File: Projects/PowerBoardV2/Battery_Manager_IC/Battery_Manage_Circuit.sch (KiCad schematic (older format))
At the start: 77 parts, among them J1 STATUS, J2 ROVER_PWR, Q1 FDG1024NZ, Q2 CSD17578Q5A, Q3 CSD17578Q5A, Q4 BSS138, SW1 SW_PUSH, U1 S-8244, U2 ATmega16HVB

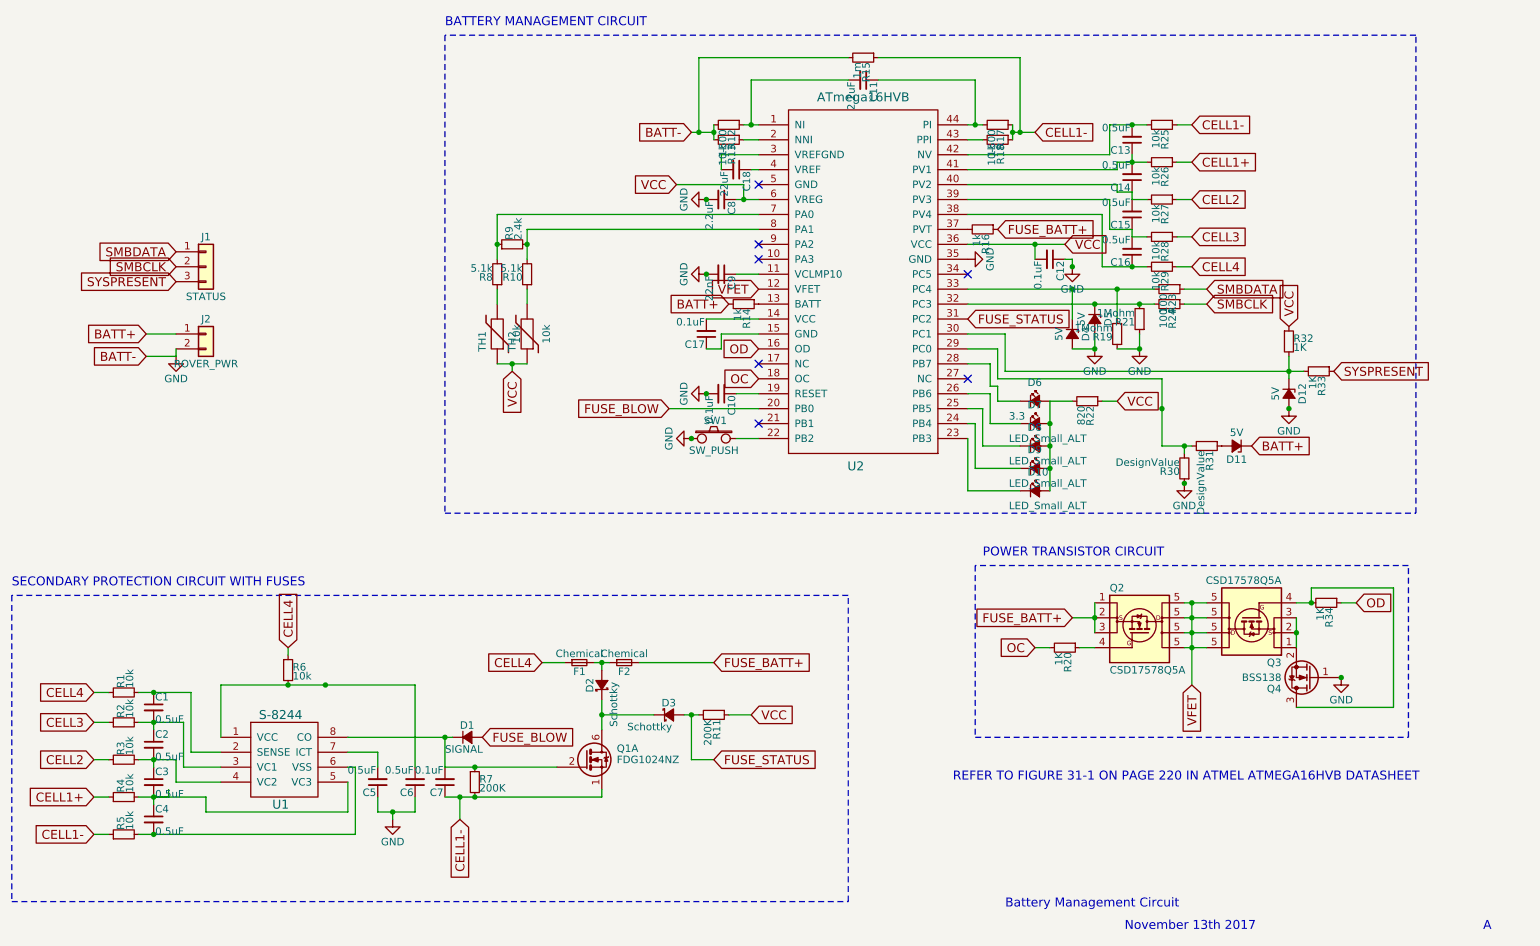
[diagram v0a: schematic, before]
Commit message: New Datasheets
Added new datasheets to the folder
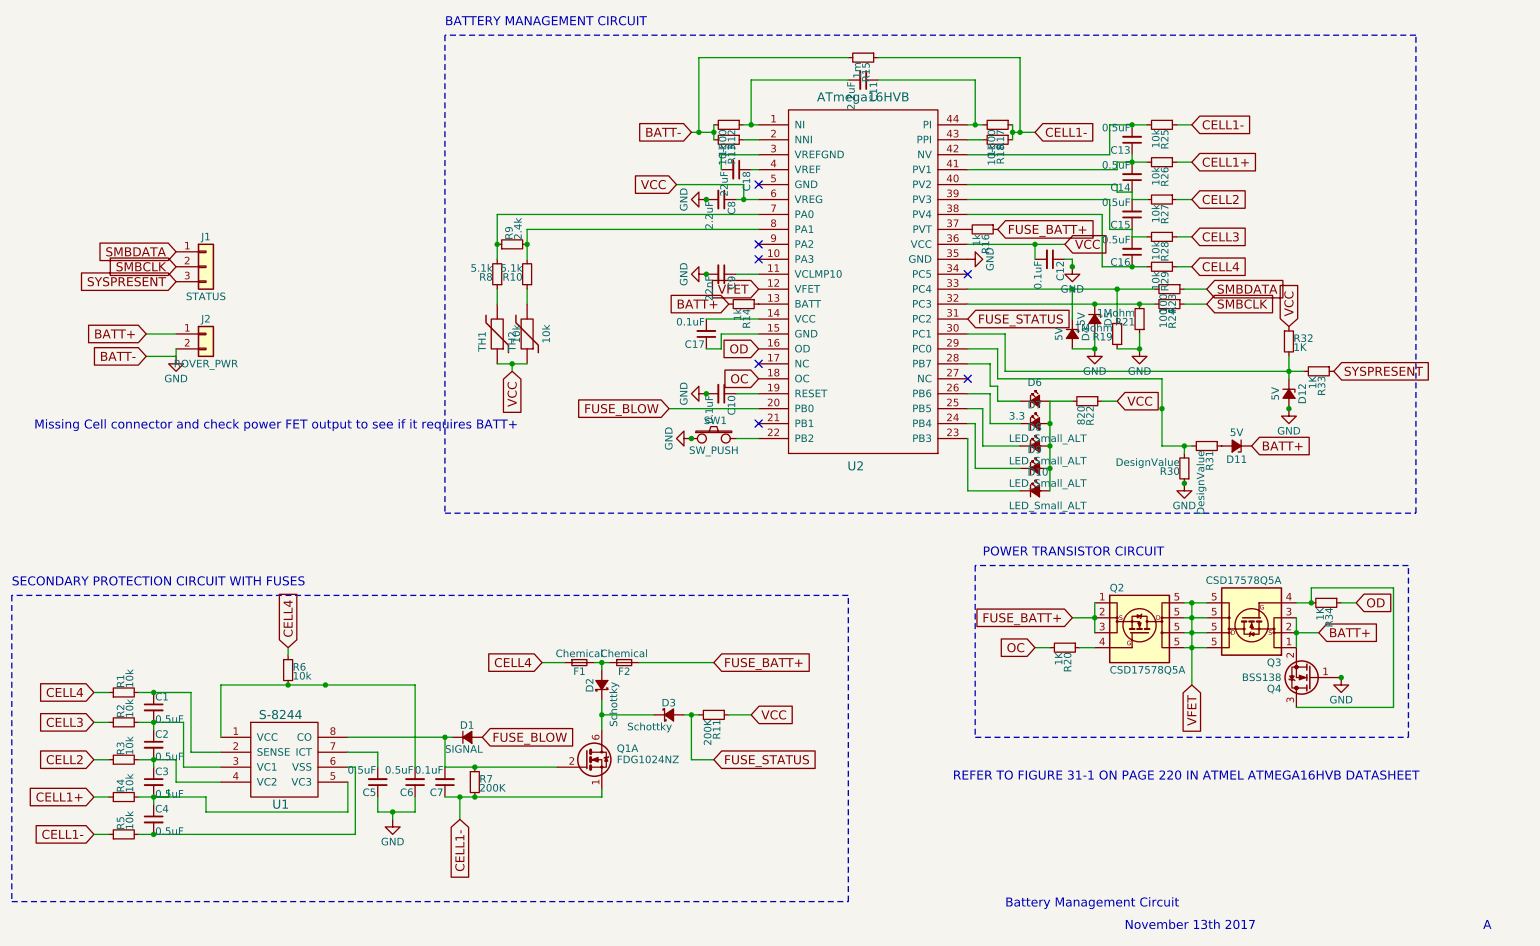
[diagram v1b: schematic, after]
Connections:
- net BATT+: now also Q3.1 (S), Q3.2 (S), Q3.3 (S), Q4.2 (S)
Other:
- note added: "Missing Cell connector and check power FET output to see if it requires BATT+"
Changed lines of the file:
@@
 Connection ~ 7800 3200
 NoConn ~ 5700 2650
+Text Notes 850  4300 0    60   ~ 0
+Missing Cell connector and check power FET output to see if it requires BATT+
+Text GLabel 9450 5650 2    60   Input ~ 0
+BATT+
+Wire Wire Line
+	9300 5650 9450 5650
 $EndSCHEMATC
